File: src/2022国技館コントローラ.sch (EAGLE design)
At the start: 46 parts

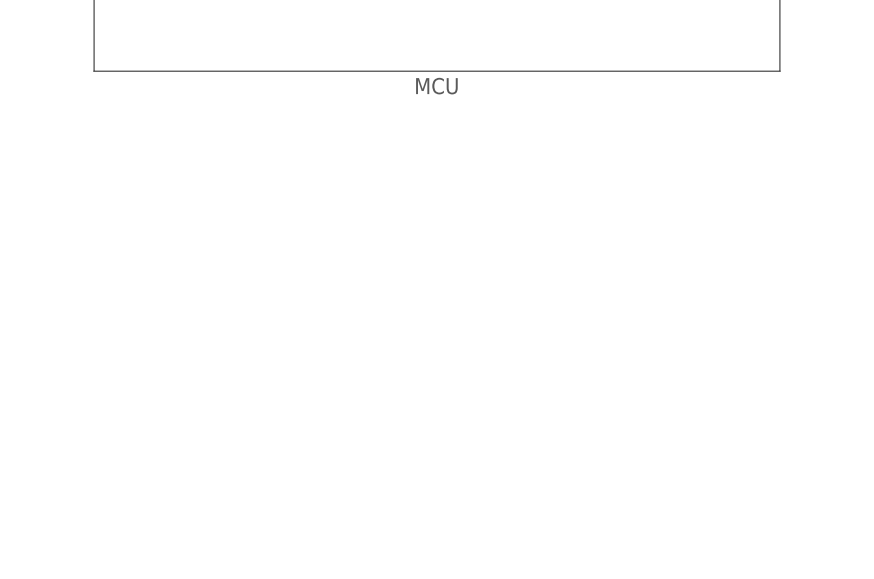
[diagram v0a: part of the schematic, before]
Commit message: 国技館コントローラの追加
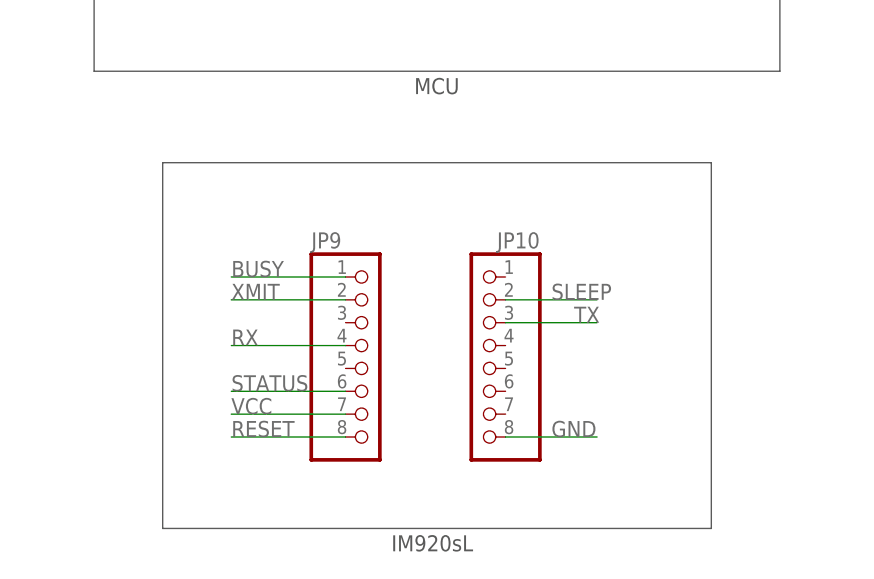
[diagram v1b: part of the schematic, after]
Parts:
- added JP10, JP9: (no value), pinhead:PINHD-1X8
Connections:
- new net BUSY: JP9.1
- new net RESET: JP9.8
- new net RX: JP9.4
- new net SLEEP: JP10.2
- new net STATUS: JP9.6
- new net TX: JP10.3
- new net VCC: JP9.7
- new net XMIT: JP9.2
- net GND: now also JP10.8
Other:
- note added: "IM920sL"
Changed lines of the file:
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@@
 <part name="SUPPLY16" library="supply2" library_urn="urn:adsk.eagle:library:372" deviceset="GND" device=""/>
 <part name="SUPPLY17" library="supply2" library_urn="urn:adsk.eagle:library:372" deviceset="GND" device=""/>
+<part name="JP9" library="pinhead" library_urn="urn:adsk.eagle:library:325" deviceset="PINHD-1X8" device="" package3d_urn="urn:adsk.eagle:package:22409/2"/>
+<part name="JP10" library="pinhead" library_urn="urn:adsk.eagle:library:325" deviceset="PINHD-1X8" device="" package3d_urn="urn:adsk.eagle:package:22409/2"/>
 </parts>
 <sheets>
@@
 <wire x1="226.06" y1="246.38" x2="152.4" y2="246.38" width="0.1524" layer="97"/>
 <text x="187.96" y="172.72" size="1.778" layer="97">LED</text>
+<wire x1="160.02" y1="71.12" x2="160.02" y2="30.48" width="0.1524" layer="97"/>
+<wire x1="160.02" y1="30.48" x2="220.98" y2="30.48" width="0.1524" layer="97"/>
+<wire x1="220.98" y1="30.48" x2="220.98" y2="71.12" width="0.1524" layer="97"/>
+<wire x1="220.98" y1="71.12" x2="160.02" y2="71.12" width="0.1524" layer="97"/>
+<text x="185.42" y="27.94" size="1.778" layer="97">IM920sL</text>
 </plain>
 <instances>
@@
 <instance part="SUPPLY17" gate="GND" x="205.74" y="181.864" smashed="yes">
 <attribute name="VALUE" x="203.835" y="178.689" size="1.778" layer="96"/>
+</instance>
+<instance part="JP9" gate="A" x="182.88" y="48.26" smashed="yes">
+<attribute name="NAME" x="176.53" y="61.595" size="1.778" layer="95"/>
+<attribute name="VALUE" x="176.53" y="35.56" size="1.778" layer="96"/>
+</instance>
+<instance part="JP10" gate="A" x="195.58" y="48.26" smashed="yes" rot="MR0">
+<attribute name="NAME" x="201.93" y="61.595" size="1.778" layer="95" rot="MR0"/>
+<attribute name="VALUE" x="201.93" y="35.56" size="1.778" layer="96" rot="MR0"/>
 </instance>
 </instances>
@@
 <wire x1="205.74" y1="185.42" x2="205.74" y2="184.404" width="0.1524" layer="91"/>
 </segment>
+<segment>
+<pinref part="JP10" gate="A" pin="8"/>
+<wire x1="198.12" y1="40.64" x2="208.28" y2="40.64" width="0.1524" layer="91"/>
+<label x="203.2" y="40.64" size="1.778" layer="95"/>
+</segment>
 </net>
 <net name="L/R1" class="0">
@@
 </segment>
 </net>
+<net name="BUSY" class="0">
+<segment>
+<pinref part="JP9" gate="A" pin="1"/>
+<wire x1="180.34" y1="58.42" x2="167.64" y2="58.42" width="0.1524" layer="91"/>
+<label x="167.64" y="58.42" size="1.778" layer="95"/>
+</segment>
+</net>
+<net name="XMIT" class="0">
+<segment>
+<pinref part="JP9" gate="A" pin="2"/>
+<wire x1="180.34" y1="55.88" x2="167.64" y2="55.88" width="0.1524" layer="91"/>
+<label x="167.64" y="55.88" size="1.778" layer="95"/>
+</segment>
+</net>
+<net name="TX" class="0">
+<segment>
+<pinref part="JP10" gate="A" pin="3"/>
+<wire x1="198.12" y1="53.34" x2="208.28" y2="53.34" width="0.1524" layer="91"/>
+<label x="205.74" y="53.34" size="1.778" layer="95"/>
+</segment>
+</net>
+<net name="RX" class="0">
+<segment>
+<pinref part="JP9" gate="A" pin="4"/>
+<wire x1="180.34" y1="50.8" x2="167.64" y2="50.8" width="0.1524" layer="91"/>
+<label x="167.64" y="50.8" size="1.778" layer="95"/>
+</segment>
+</net>
+<net name="STATUS" class="0">
+<segment>
+<pinref part="JP9" gate="A" pin="6"/>
+<wire x1="180.34" y1="45.72" x2="167.64" y2="45.72" width="0.1524" layer="91"/>
+<label x="167.64" y="45.72" size="1.778" layer="95"/>
+</segment>
+</net>
+<net name="VCC" class="0">
+<segment>
+<pinref part="JP9" gate="A" pin="7"/>
+<wire x1="180.34" y1="43.18" x2="167.64" y2="43.18" width="0.1524" layer="91"/>
+<label x="167.64" y="43.18" size="1.778" layer="95"/>
+</segment>
+</net>
+<net name="RESET" class="0">
+<segment>
+<pinref part="JP9" gate="A" pin="8"/>
+<wire x1="180.34" y1="40.64" x2="167.64" y2="40.64" width="0.1524" layer="91"/>
+<label x="167.64" y="40.64" size="1.778" layer="95"/>
+</segment>
+</net>
+<net name="SLEEP" class="0">
+<segment>
+<pinref part="JP10" gate="A" pin="2"/>
+<wire x1="198.12" y1="55.88" x2="208.28" y2="55.88" width="0.1524" layer="91"/>
+<label x="203.2" y="55.88" size="1.778" layer="95"/>
+</segment>
+</net>

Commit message: 「ｋ」コントローラ
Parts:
- added JP11, JP12: (no value), con-jst-xh (1):05-JST
- added SV1, SV2: (no value), con-ml:ML10
- added U$15: 02-JST, con-jst-xh (1):02-JST
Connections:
- removed net VCC: JP9.7
- new net VIN: F411RE_LEFT.24, U$15.2
- net 3V3: now also F411RE_LEFT.16, JP9.7, SV1.2, SV2.2
- net BL1: now also F411RE_RIGHT.11
- net BL2: now also F411RE_RIGHT.13
- net BR1: now also F411RE_RIGHT.23
- net BR2: now also F411RE_RIGHT.25
- net BUSY: now also F411RE_RIGHT.24, SV1.10, SV2.10
- net CK1_DOWN: now also F411RE_RIGHT.21, U$4.1; no longer U$5.1
- net CK1_LEFT: now also F411RE_RIGHT.15
- net CK1_RIGHT: now also F411RE_RIGHT.17, U$5.1; no longer U$6.1
- net CK1_UP: now also F411RE_RIGHT.19, U$6.1; no longer U$4.1
- net CK2_DOWN: now also F411RE_RIGHT.33, U$10.1; no longer U$9.1
- net CK2_LEFT: now also F411RE_RIGHT.27, U$7.1; no longer U$8.1
- net CK2_RIGHT: now also F411RE_RIGHT.29, U$9.1; no longer U$10.1
- net CK2_UP: now also F411RE_RIGHT.31, U$8.1; no longer U$7.1
- net GND: now also F411RE_LEFT.8, SV1.3, SV2.3, U$15.1
- net L/R1: now also F411RE_LEFT.28
- net L/R2: now also F411RE_LEFT.32
- net LED1: now also F411RE_RIGHT.1, JP11.1, JP12.1
- net LED2: now also F411RE_RIGHT.3, JP11.2, JP12.2
- net LED3: now also F411RE_RIGHT.5, JP11.3, JP12.3
- net LED4: now also F411RE_RIGHT.2, JP11.4, JP12.4
- net LED5: now also F411RE_RIGHT.4, JP11.5, JP12.5
- net RESET: now also F411RE_RIGHT.30, SV1.9, SV2.9
- net RX: now also F411RE_LEFT.21, SV1.6, SV2.6
- net SLEEP: now also F411RE_RIGHT.22, SV1.7, SV2.7
- net STATUS: now also F411RE_RIGHT.28, SV1.4, SV2.4
- net TX: now also F411RE_LEFT.17, SV1.5, SV2.5
- net U/D1: now also F411RE_LEFT.30
- net U/D2: now also F411RE_LEFT.34
- net XMIT: now also F411RE_RIGHT.26, SV1.8, SV2.8
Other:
- note added: "External Charging"
- note added: "MILコネ"
- moved on the sheet: F411RE_LEFT, F411RE_RIGHT, LED1, LED2, LED3, LED4, LED5, R13, R14, R15, R16, R17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

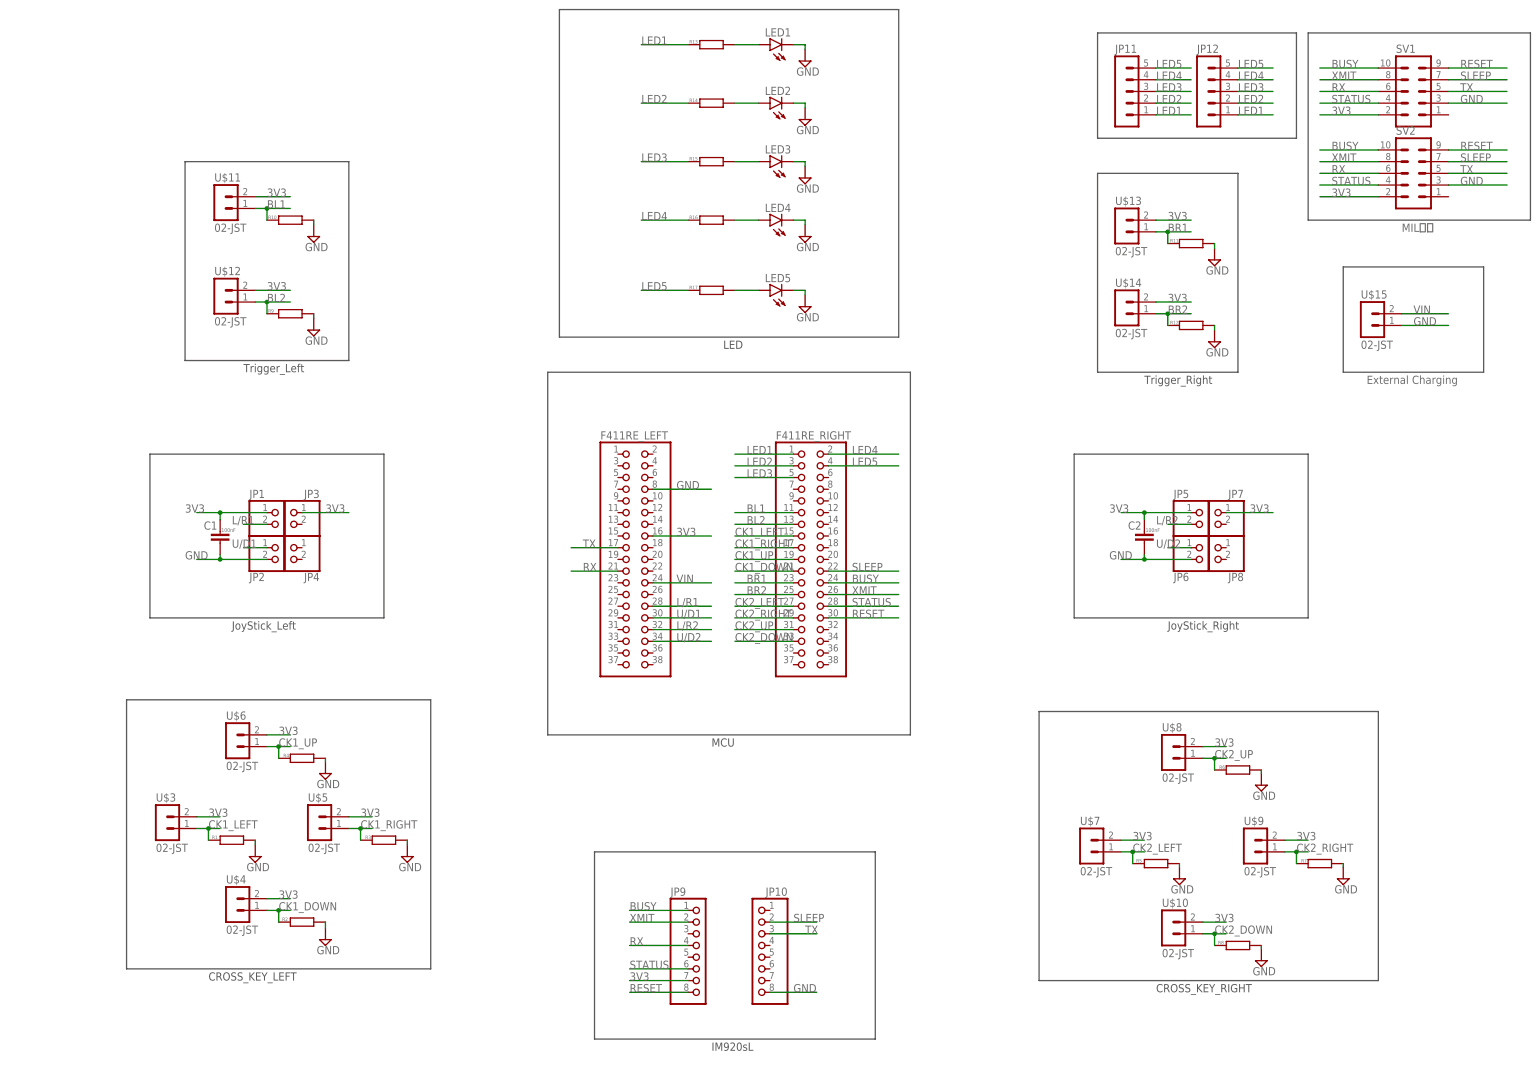
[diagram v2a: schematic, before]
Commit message: 国技館コントローラ_配線の修正
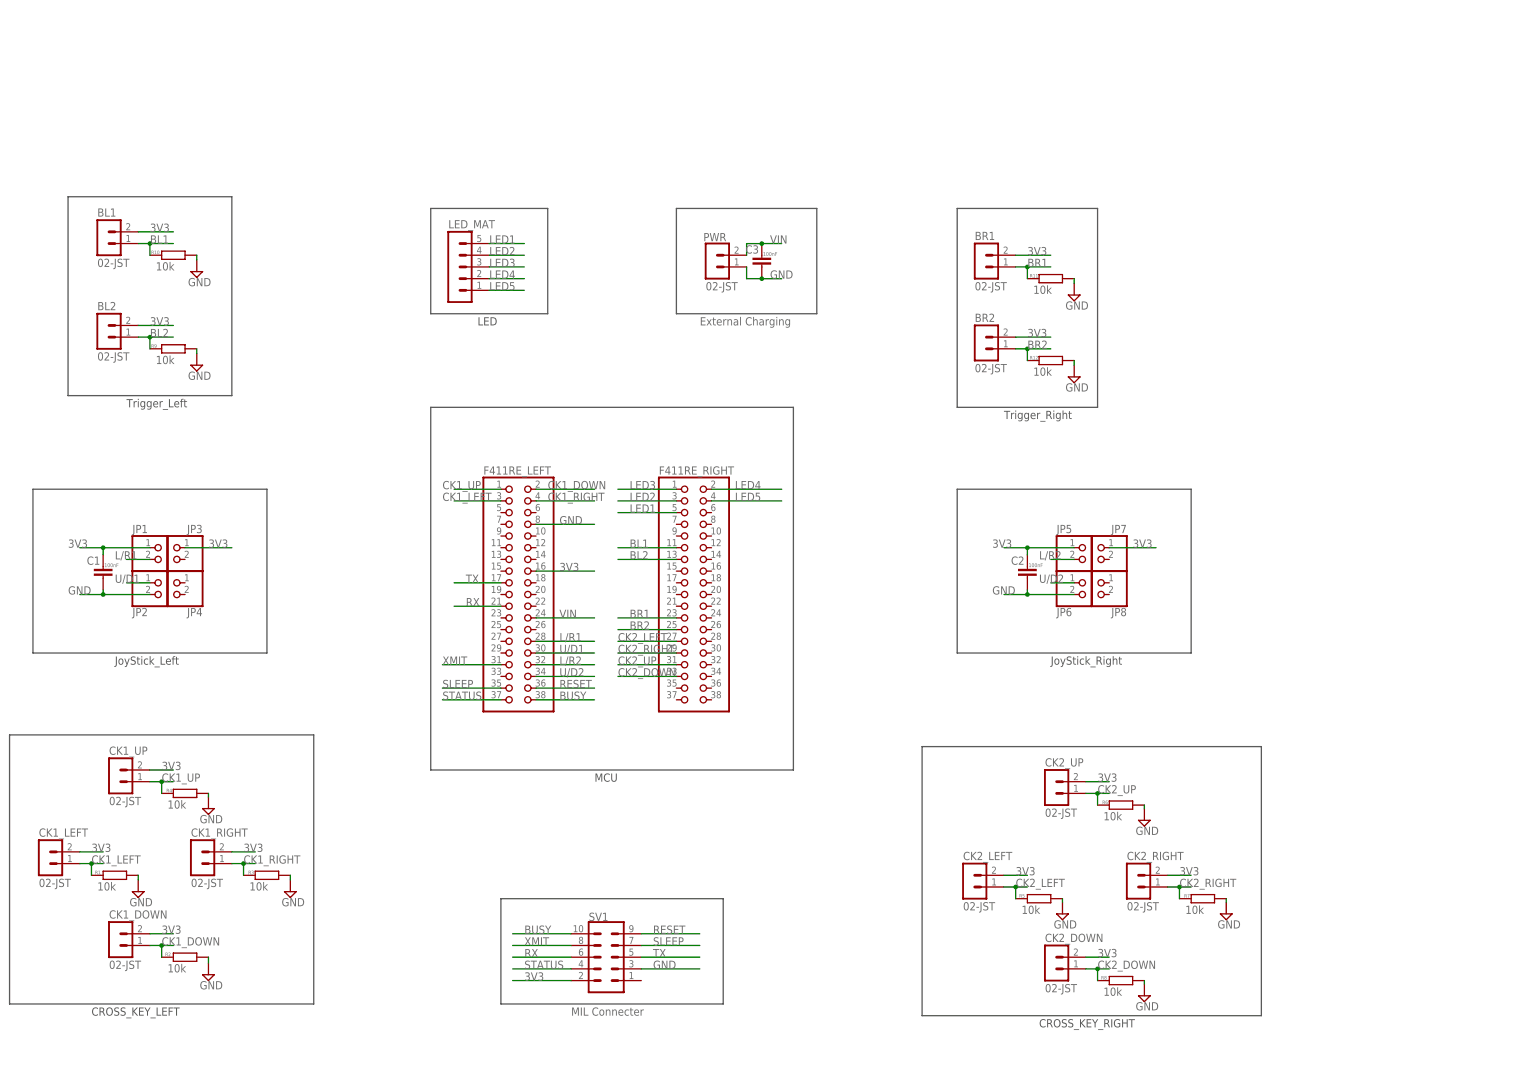
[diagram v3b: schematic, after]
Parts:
- removed JP10, JP9: (no value), pinhead:PINHD-1X8
- removed JP11, JP12: (no value), con-jst-xh (1):05-JST
- removed LED1, LED2, LED3, LED4, LED5: (no value), led:LED5MM
- removed R13, R14, R15, R16, R17: (no value), rcl:R-EU_0204/7
- removed SV2: (no value), con-ml:ML10
- removed U$10, U$11, U$12, U$13, U$14, U$3, U$4, U$5, U$6, U$7, U$8, U$9: 02-JST, con-jst-xh:02-JST
- removed U$15: 02-JST, con-jst-xh (1):02-JST
- added BL1, BL2, BR1, BR2, CK1_DOWN, CK1_LEFT, CK1_RIGHT, CK1_UP, CK2_DOWN, CK2_LEFT, CK2_RIGHT, CK2_UP: 02-JST, con-jst-xh:02-JST
- added C3: 100nF, rcl:C-EU025-024X044
- added LED_MAT: (no value), con-jst-xh (1):05-JST
- added PWR: 02-JST, con-jst-xh (1):02-JST
- R1, R10, R11, R12, R2, R3, R4, R5, R6, R7, R8, R9: value (none) -> 10k
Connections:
- removed net N$10: LED5.A, R17.2
- removed net N$6: LED1.A, R13.2
- removed net N$7: LED2.A, R14.2
- removed net N$8: LED3.A, R15.2
- removed net N$9: LED4.A, R16.2
- net 3V3: now also BL1.2, BL2.2, BR1.2, BR2.2, CK1_DOWN.2, CK1_LEFT.2, CK1_RIGHT.2, CK1_UP.2, CK2_DOWN.2, CK2_LEFT.2, CK2_RIGHT.2, CK2_UP.2; no longer JP9.7, SV2.2, U$10.2, U$11.2, U$12.2, U$13.2, U$14.2, U$3.2, U$4.2, U$5.2, U$6.2, U$7.2, U$8.2, U$9.2
- net BL1: now also BL1.1; no longer U$11.1
- net BL2: now also BL2.1; no longer U$12.1
- net BR1: now also BR1.1; no longer U$13.1
- net BR2: now also BR2.1; no longer U$14.1
- net BUSY: now also F411RE_LEFT.38; no longer F411RE_RIGHT.24, JP9.1, SV2.10
- net CK1_DOWN: now also CK1_DOWN.1, F411RE_LEFT.2; no longer F411RE_RIGHT.21, U$4.1
- net CK1_LEFT: now also CK1_LEFT.1, F411RE_LEFT.3; no longer F411RE_RIGHT.15, U$3.1
- net CK1_RIGHT: now also CK1_RIGHT.1, F411RE_LEFT.4; no longer F411RE_RIGHT.17, U$5.1
- net CK1_UP: now also CK1_UP.1, F411RE_LEFT.1; no longer F411RE_RIGHT.19, U$6.1
- net CK2_DOWN: now also CK2_DOWN.1; no longer U$10.1
- net CK2_LEFT: now also CK2_LEFT.1; no longer U$7.1
- net CK2_RIGHT: now also CK2_RIGHT.1; no longer U$9.1
- net CK2_UP: now also CK2_UP.1; no longer U$8.1
- net GND: now also C3.2, PWR.1; no longer JP10.8, LED1.C, LED2.C, LED3.C, LED4.C, LED5.C, SV2.3, U$15.1
- net LED1: now also F411RE_RIGHT.5, LED_MAT.5; no longer F411RE_RIGHT.1, JP11.1, JP12.1, R13.1
- net LED2: now also LED_MAT.4; no longer JP11.2, JP12.2, R14.1
- net LED3: now also F411RE_RIGHT.1, LED_MAT.3; no longer F411RE_RIGHT.5, JP11.3, JP12.3, R15.1
- net LED4: now also LED_MAT.2; no longer JP11.4, JP12.4, R16.1
- net LED5: now also LED_MAT.1; no longer JP11.5, JP12.5, R17.1
- net RESET: now also F411RE_LEFT.36; no longer F411RE_RIGHT.30, JP9.8, SV2.9
- net RX: no longer JP9.4, SV2.6
- net SLEEP: now also F411RE_LEFT.35; no longer F411RE_RIGHT.22, JP10.2, SV2.7
- net STATUS: now also F411RE_LEFT.37; no longer F411RE_RIGHT.28, JP9.6, SV2.4
- net TX: no longer JP10.3, SV2.5
- net VIN: now also C3.1, PWR.2; no longer U$15.2
- net XMIT: now also F411RE_LEFT.31; no longer F411RE_RIGHT.26, JP9.2, SV2.8
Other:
- note added: "MIL Connecter"
- note removed: "IM920sL"
- note removed: "MILコネ"
- moved on the sheet: C1, C2, F411RE_LEFT, F411RE_RIGHT, JP1, JP2, JP3, JP4, JP5, JP6, JP7, JP8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

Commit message: [k]コントローラ
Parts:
- added U$3, U$4: 02-JST, con-jst-xh (1):02-JST
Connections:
- net 3V3: now also F411RE_RIGHT.7, SV1.3; no longer SV1.2
- net BL1: now also F411RE_RIGHT.28; no longer F411RE_RIGHT.11
- net BL2: now also F411RE_RIGHT.30; no longer F411RE_RIGHT.13
- net BR1: now also F411RE_RIGHT.24; no longer F411RE_RIGHT.23
- net BR2: now also F411RE_RIGHT.26; no longer F411RE_RIGHT.25
- net GND: now also F411RE_LEFT.19, F411RE_LEFT.22, F411RE_RIGHT.20, SV1.7; no longer SV1.3
- net L/R2: now also U$3.2, U$4.2
- net RX: now also SV1.2; no longer SV1.6
- net SLEEP: now also SV1.6; no longer SV1.7
- net STATUS: now also SV1.8; no longer SV1.4
- net U/D2: now also U$3.1, U$4.1
- net XMIT: now also SV1.4; no longer SV1.8
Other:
- note added: "Analogpin"
- moved on the sheet: BL1, BL2, BR1, BR2, C3, LED_MAT, PWR, R10, R11, R12, R9

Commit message: 国技館足回り修正前
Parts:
- removed LED_MAT: (no value), con-jst-xh (1):05-JST
- added EMERGENCY: (no value), con-jst-xh:03-JST
- added LED: (no value), con-jst-xh:06-JST
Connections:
- new net EME_SW: EMERGENCY.2, F411RE_LEFT.13
- net 3V3: now also EMERGENCY.3
- net GND: now also EMERGENCY.1, LED.1
- net LED1: now also LED.6; no longer LED_MAT.5
- net LED2: now also LED.5; no longer LED_MAT.4
- net LED3: now also LED.4; no longer LED_MAT.3
- net LED4: now also LED.3; no longer LED_MAT.2
- net LED5: now also LED.2; no longer LED_MAT.1
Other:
- note added: "EMERGENCY"
- moved on the sheet: BL1, BL2, BR1, BR2, C1, C2, C3, CK1_DOWN, CK1_LEFT, CK1_RIGHT, CK1_UP, CK2_DOWN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
